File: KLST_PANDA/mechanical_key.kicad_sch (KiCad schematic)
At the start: 4 parts, among them SW5 BUTTON

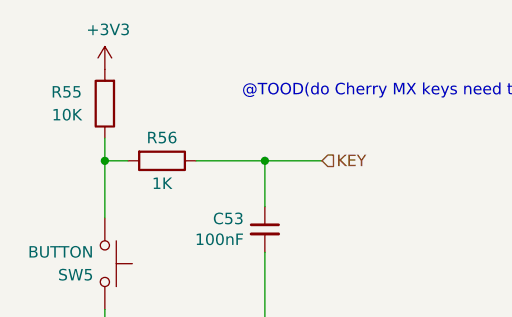
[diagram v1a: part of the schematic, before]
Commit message: started cleaning up schematic ( addressing DRC errors/warning ) (WIP)
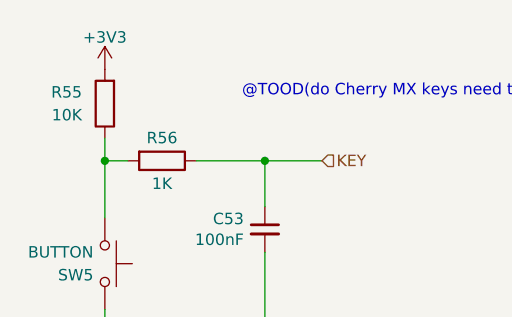
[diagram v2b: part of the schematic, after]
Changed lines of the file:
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@@
       (effects (font (size 1.27 1.27)) hide)
     )
-    (property "Value" "+3V3" (at 134.366 81.3308 0)
+    (property "Value" "+3V3" (at 133.985 82.169 0)
       (effects (font (size 1.27 1.27)))
     )
@@
         )
         (path "/b4513875-4c57-4720-bcc5-43ead67fe18f/f08ee185-46fd-4c64-8c0d-73017bc497ee/042452de-70bc-4b43-b264-a9a1cbea3e51"
-          (reference "#PWR090") (unit 1)
+          (reference "#PWR091") (unit 1)
         )
         (path "/b4513875-4c57-4720-bcc5-43ead67fe18f/f08ee185-46fd-4c64-8c0d-73017bc497ee/84723a09-c269-4794-b0be-89f4260a1140"
-          (reference "#PWR092") (unit 1)
+          (reference "#PWR093") (unit 1)
         )
       )
@@
         )
         (path "/b4513875-4c57-4720-bcc5-43ead67fe18f/f08ee185-46fd-4c64-8c0d-73017bc497ee/042452de-70bc-4b43-b264-a9a1cbea3e51"
-          (reference "#PWR091") (unit 1)
+          (reference "#PWR092") (unit 1)
         )
         (path "/b4513875-4c57-4720-bcc5-43ead67fe18f/f08ee185-46fd-4c64-8c0d-73017bc497ee/84723a09-c269-4794-b0be-89f4260a1140"
-          (reference "#PWR093") (unit 1)
+          (reference "#PWR094") (unit 1)
         )
       )

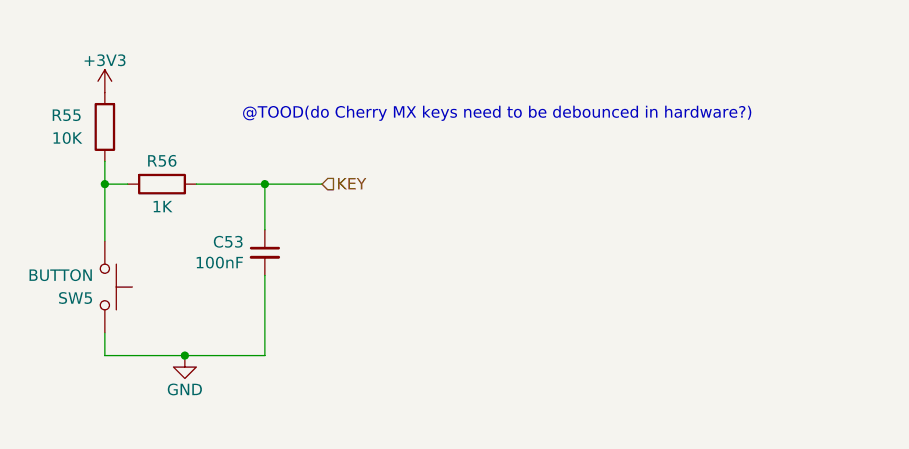
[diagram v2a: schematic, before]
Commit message: removed DRC warnings and error, added power page
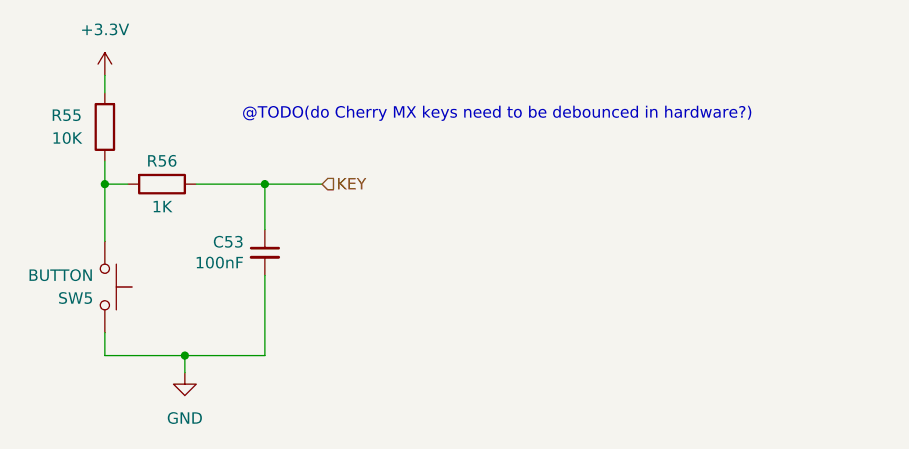
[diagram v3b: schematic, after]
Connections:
- net +3V3 renamed +3.3V
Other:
- note added: "@TODO(do Cherry MX keys need to be debounced in hardware?)"
- note removed: "@TOOD(do Cherry MX keys need to be debounced in hardware?)"
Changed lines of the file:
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@@
 (kicad_sch (version 20230121) (generator eeschema)
   (paper "A4")
+  (junction (at 133.985 95.885) (diameter 0) (color 0 0 0 0)
+  )
+  (junction (at 151.765 95.885) (diameter 0) (color 0 0 0 0)
+  )
   (junction (at 142.875 114.935) (diameter 0) (color 0 0 0 0)
   )
-  (junction (at 133.985 95.885) (diameter 0) (color 0 0 0 0)
-  )
-  (junction (at 151.765 95.885) (diameter 0) (color 0 0 0 0)
+  (wire (pts (xy 133.985 83.82) (xy 133.985 85.725))
+    (stroke (width 0) (type default))
+  )
+  (wire (pts (xy 142.875 114.935) (xy 151.765 114.935))
+    (stroke (width 0) (type default))
   )
   (wire (pts (xy 133.985 114.935) (xy 142.875 114.935))
@@
     (stroke (width 0) (type default))
   )
-  (wire (pts (xy 142.875 114.935) (xy 151.765 114.935))
-    (stroke (width 0) (type default))
-  )
   (wire (pts (xy 151.765 106.045) (xy 151.765 114.935))
     (stroke (width 0) (type default))
   )
+  (wire (pts (xy 142.875 114.935) (xy 142.875 116.84))
+    (stroke (width 0) (type default))
+  )
   (wire (pts (xy 144.145 95.885) (xy 151.765 95.885))
     (stroke (width 0) (type default))
@@
     (stroke (width 0) (type default))
   )
-  (text "@TOOD(do Cherry MX keys need to be debounced in hardware?)"
+  (text "@TODO(do Cherry MX keys need to be debounced in hardware?)"
     (at 149.225 88.9 0)
     (effects (font (size 1.27 1.27)) (justify left bottom))
@@
     (effects (font (size 1.27 1.27)) (justify left))
   )
-  (symbol (lib_id "power:+3V3") (at 133.985 85.725 0) (unit 1)
-    (in_bom yes) (on_board yes) (dnp no)
-    (property "Reference" "#PWR080" (at 133.985 89.535 0)
-      (effects (font (size 1.27 1.27)) hide)
-    )
-    (property "Value" "+3V3" (at 133.985 82.169 0)
-      (effects (font (size 1.27 1.27)))
-    )
-    (property "Footprint" "" (at 133.985 85.725 0)
-      (effects (font (size 1.27 1.27)) hide)
-    )
-    (property "Datasheet" "" (at 133.985 85.725 0)
-      (effects (font (size 1.27 1.27)) hide)
-    )
-    (pin "1")
-    (instances
-      (project "KLST_SHEEP"
-        (path "/7c1fd6fc-5c53-4ccb-a456-46fe6fc0bc71/00000000-0000-0000-0000-00006058fda0"
-          (reference "#PWR080") (unit 1)
-        )
-      )
-      (project "KLST_PANDA"
-        (path "/b4513875-4c57-4720-bcc5-43ead67fe18f/f08ee185-46fd-4c64-8c0d-73017bc497ee/7936a5e0-5a04-43e4-aa84-42432289d154"
-          (reference "#PWR071") (unit 1)
-        )
-        (path "/b4513875-4c57-4720-bcc5-43ead67fe18f/f08ee185-46fd-4c64-8c0d-73017bc497ee"
-          (reference "#PWR?") (unit 1)
-        )
-        (path "/b4513875-4c57-4720-bcc5-43ead67fe18f/f08ee185-46fd-4c64-8c0d-73017bc497ee/042452de-70bc-4b43-b264-a9a1cbea3e51"
-          (reference "#PWR091") (unit 1)
-        )
-        (path "/b4513875-4c57-4720-bcc5-43ead67fe18f/f08ee185-46fd-4c64-8c0d-73017bc497ee/84723a09-c269-4794-b0be-89f4260a1140"
-          (reference "#PWR093") (unit 1)
-        )
-      )
-    )
-  )
-  (symbol (lib_id "power:GND") (at 142.875 114.935 0) (unit 1)
-    (in_bom yes) (on_board yes) (dnp no)
-    (property "Reference" "#PWR081" (at 142.875 121.285 0)
-      (effects (font (size 1.27 1.27)) hide)
-    )
-    (property "Value" "GND" (at 142.875 118.745 0)
-      (effects (font (size 1.27 1.27)))
-    )
-    (property "Footprint" "" (at 142.875 114.935 0)
-      (effects (font (size 1.27 1.27)) hide)
-    )
-    (property "Datasheet" "" (at 142.875 114.935 0)
-      (effects (font (size 1.27 1.27)) hide)
-    )
-    (pin "1")
-    (instances
-      (project "KLST_SHEEP"
-        (path "/7c1fd6fc-5c53-4ccb-a456-46fe6fc0bc71/00000000-0000-0000-0000-00006058fda0"
-          (reference "#PWR081") (unit 1)
-        )
-      )
-      (project "KLST_PANDA"
-        (path "/b4513875-4c57-4720-bcc5-43ead67fe18f/f08ee185-46fd-4c64-8c0d-73017bc497ee/7936a5e0-5a04-43e4-aa84-42432289d154"
-          (reference "#PWR072") (unit 1)
-        )
-        (path "/b4513875-4c57-4720-bcc5-43ead67fe18f/f08ee185-46fd-4c64-8c0d-73017bc497ee"
-          (reference "#PWR?") (unit 1)
-        )
-        (path "/b4513875-4c57-4720-bcc5-43ead67fe18f/f08ee185-46fd-4c64-8c0d-73017bc497ee/042452de-70bc-4b43-b264-a9a1cbea3e51"
-          (reference "#PWR092") (unit 1)
-        )
-        (path "/b4513875-4c57-4720-bcc5-43ead67fe18f/f08ee185-46fd-4c64-8c0d-73017bc497ee/84723a09-c269-4794-b0be-89f4260a1140"
-          (reference "#PWR094") (unit 1)
+  (symbol (lib_id "power:+3.3V") (at 133.985 83.82 0) (unit 1)
+    (in_bom yes) (on_board yes) (dnp no) (fields_autoplaced)
+    (property "Reference" "#PWR077" (at 133.985 87.63 0)
+      (effects (font (size 1.27 1.27)) hide)
+    )
+    (property "Value" "+3.3V" (at 133.985 78.74 0)
+      (effects (font (size 1.27 1.27)))
+    )
+    (property "Footprint" "" (at 133.985 83.82 0)
+      (effects (font (size 1.27 1.27)) hide)
+    )
+    (property "Datasheet" "" (at 133.985 83.82 0)
+      (effects (font (size 1.27 1.27)) hide)
+    )
+    (pin "1")
+    (instances
+      (project "KLST_PANDA"
+        (path "/b4513875-4c57-4720-bcc5-43ead67fe18f/47e8e77e-c64e-4c44-bfd8-2073580a3d85"
+          (reference "#PWR077") (unit 1)
+        )
+        (path "/b4513875-4c57-4720-bcc5-43ead67fe18f/f08ee185-46fd-4c64-8c0d-73017bc497ee/042452de-70bc-4b43-b264-a9a1cbea3e51"
+          (reference "#PWR082") (unit 1)
+        )
+        (path "/b4513875-4c57-4720-bcc5-43ead67fe18f/f08ee185-46fd-4c64-8c0d-73017bc497ee/84723a09-c269-4794-b0be-89f4260a1140"
+          (reference "#PWR084") (unit 1)
+        )
+      )
+    )
+  )
+  (symbol (lib_id "power:GND") (at 142.875 116.84 0) (unit 1)
+    (in_bom yes) (on_board yes) (dnp no) (fields_autoplaced)
+    (property "Reference" "#PWR083" (at 142.875 123.19 0)
+      (effects (font (size 1.27 1.27)) hide)
+    )
+    (property "Value" "GND" (at 142.875 121.92 0)
+      (effects (font (size 1.27 1.27)))
+    )
+    (property "Footprint" "" (at 142.875 116.84 0)
+      (effects (font (size 1.27 1.27)) hide)
+    )
+    (property "Datasheet" "" (at 142.875 116.84 0)
+      (effects (font (size 1.27 1.27)) hide)
+    )
+    (pin "1")
+    (instances
+      (project "KLST_PANDA"
+        (path "/b4513875-4c57-4720-bcc5-43ead67fe18f/f08ee185-46fd-4c64-8c0d-73017bc497ee/042452de-70bc-4b43-b264-a9a1cbea3e51"
+          (reference "#PWR083") (unit 1)
+        )
+        (path "/b4513875-4c57-4720-bcc5-43ead67fe18f/f08ee185-46fd-4c64-8c0d-73017bc497ee/84723a09-c269-4794-b0be-89f4260a1140"
+          (reference "#PWR085") (unit 1)
         )
       )
@@
         )
         (path "/b4513875-4c57-4720-bcc5-43ead67fe18f/f08ee185-46fd-4c64-8c0d-73017bc497ee/042452de-70bc-4b43-b264-a9a1cbea3e51"
-          (reference "C71") (unit 1)
-        )
-        (path "/b4513875-4c57-4720-bcc5-43ead67fe18f/f08ee185-46fd-4c64-8c0d-73017bc497ee/84723a09-c269-4794-b0be-89f4260a1140"
-          (reference "C72") (unit 1)
+          (reference "C47") (unit 1)
+        )
+        (path "/b4513875-4c57-4720-bcc5-43ead67fe18f/f08ee185-46fd-4c64-8c0d-73017bc497ee/84723a09-c269-4794-b0be-89f4260a1140"
+          (reference "C48") (unit 1)
         )
       )
@@
         )
         (path "/b4513875-4c57-4720-bcc5-43ead67fe18f/f08ee185-46fd-4c64-8c0d-73017bc497ee/042452de-70bc-4b43-b264-a9a1cbea3e51"
-          (reference "R67") (unit 1)
-        )
-        (path "/b4513875-4c57-4720-bcc5-43ead67fe18f/f08ee185-46fd-4c64-8c0d-73017bc497ee/84723a09-c269-4794-b0be-89f4260a1140"
-          (reference "R69") (unit 1)
+          (reference "R53") (unit 1)
+        )
+        (path "/b4513875-4c57-4720-bcc5-43ead67fe18f/f08ee185-46fd-4c64-8c0d-73017bc497ee/84723a09-c269-4794-b0be-89f4260a1140"
+          (reference "R55") (unit 1)
         )
       )
@@
         )
         (path "/b4513875-4c57-4720-bcc5-43ead67fe18f/f08ee185-46fd-4c64-8c0d-73017bc497ee/042452de-70bc-4b43-b264-a9a1cbea3e51"
-          (reference "R68") (unit 1)
-        )
-        (path "/b4513875-4c57-4720-bcc5-43ead67fe18f/f08ee185-46fd-4c64-8c0d-73017bc497ee/84723a09-c269-4794-b0be-89f4260a1140"
-          (reference "R70") (unit 1)
-        )
-      )
+          (reference "R54") (unit 1)
+        )
+        (path "/b4513875-4c57-4720-bcc5-43ead67fe18f/f08ee185-46fd-4c64-8c0d-73017bc497ee/84723a09-c269-4794-b0be-89f4260a1140"
+          (reference "R56") (unit 1)
+        )
+      )

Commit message: cleaned up
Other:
- moved on the sheet: C53, R56, SW5
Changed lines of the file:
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@@
     (stroke (width 0) (type default))
   )
-  (wire (pts (xy 151.765 95.885) (xy 151.765 100.965))
-    (stroke (width 0) (type default))
-  )
-  (wire (pts (xy 151.765 106.045) (xy 151.765 114.935))
+  (wire (pts (xy 151.765 95.885) (xy 151.765 102.87))
+    (stroke (width 0) (type default))
+  )
+  (wire (pts (xy 151.765 107.95) (xy 151.765 114.935))
     (stroke (width 0) (type default))
   )
@@
     (stroke (width 0) (type default))
   )
-  (wire (pts (xy 144.145 95.885) (xy 151.765 95.885))
-    (stroke (width 0) (type default))
-  )
-  (wire (pts (xy 133.985 95.885) (xy 133.985 102.235))
-    (stroke (width 0) (type default))
-  )
-  (wire (pts (xy 133.985 114.935) (xy 133.985 112.395))
-    (stroke (width 0) (type default))
-  )
-  (wire (pts (xy 136.525 95.885) (xy 133.985 95.885))
+  (wire (pts (xy 146.685 95.885) (xy 151.765 95.885))
+    (stroke (width 0) (type default))
+  )
+  (wire (pts (xy 133.985 95.885) (xy 133.985 100.33))
+    (stroke (width 0) (type default))
+  )
+  (wire (pts (xy 133.985 114.935) (xy 133.985 110.49))
+    (stroke (width 0) (type default))
+  )
+  (wire (pts (xy 139.065 95.885) (xy 133.985 95.885))
     (stroke (width 0) (type default))
   )
@@
     )
   )
-  (symbol (lib_id "Switch:SW_Push") (at 133.985 107.315 270) (unit 1)
-    (in_bom yes) (on_board yes) (dnp no)
-    (property "Reference" "SW5" (at 132.715 108.585 90)
+  (symbol (lib_id "Switch:SW_Push") (at 133.985 105.41 270) (unit 1)
+    (in_bom yes) (on_board yes) (dnp no)
+    (property "Reference" "SW5" (at 132.715 106.68 90)
       (effects (font (size 1.27 1.27)) (justify right))
     )
-    (property "Value" "BUTTON" (at 132.715 106.045 90)
+    (property "Value" "BUTTON" (at 132.715 104.14 90)
       (effects (font (size 1.27 1.27)) (justify right))
     )
-    (property "Footprint" "Cherry_MX:SW_Cherry_MX_PCB" (at 139.065 107.315 0)
-      (effects (font (size 1.27 1.27)) hide)
-    )
-    (property "Datasheet" "~" (at 139.065 107.315 0)
+    (property "Footprint" "Cherry_MX:SW_Cherry_MX_PCB" (at 139.065 105.41 0)
+      (effects (font (size 1.27 1.27)) hide)
+    )
+    (property "Datasheet" "~" (at 139.065 105.41 0)
       (effects (font (size 1.27 1.27)) hide)
     )
@@
     )
   )
-  (symbol (lib_id "Device:C_Small") (at 151.765 103.505 0) (mirror y) (unit 1)
-    (in_bom yes) (on_board yes) (dnp no)
-    (property "Reference" "C53" (at 149.4282 102.3366 0)
-      (effects (font (size 1.27 1.27)) (justify left))
-    )
-    (property "Value" "100nF" (at 149.4282 104.648 0)
-      (effects (font (size 1.27 1.27)) (justify left))
-    )
-    (property "Footprint" "Capacitor_SMD:C_0402_1005Metric" (at 151.765 103.505 0)
-      (effects (font (size 1.27 1.27)) hide)
-    )
-    (property "Datasheet" "~" (at 151.765 103.505 0)
-      (effects (font (size 1.27 1.27)) hide)
-    )
-    (property "MFR.Part #" "CL05B104KO5NNNC" (at 151.765 103.505 0)
-      (effects (font (size 1.27 1.27)) hide)
-    )
-    (property "LCSC Part #" "" (at 151.765 103.505 0)
-      (effects (font (size 1.27 1.27)) hide)
-    )
-    (property "Extended Part" "-" (at 151.765 103.505 0)
-      (effects (font (size 1.27 1.27)) hide)
-    )
-    (property "JLCPCB Part #" "C1525" (at 151.765 103.505 0)
+  (symbol (lib_id "Device:C_Small") (at 151.765 105.41 0) (mirror y) (unit 1)
+    (in_bom yes) (on_board yes) (dnp no)
+    (property "Reference" "C53" (at 149.4282 104.2416 0)
+      (effects (font (size 1.27 1.27)) (justify left))
+    )
+    (property "Value" "100nF" (at 149.4282 106.553 0)
+      (effects (font (size 1.27 1.27)) (justify left))
+    )
+    (property "Footprint" "Capacitor_SMD:C_0402_1005Metric" (at 151.765 105.41 0)
+      (effects (font (size 1.27 1.27)) hide)
+    )
+    (property "Datasheet" "~" (at 151.765 105.41 0)
+      (effects (font (size 1.27 1.27)) hide)
+    )
+    (property "MFR.Part #" "CL05B104KO5NNNC" (at 151.765 105.41 0)
+      (effects (font (size 1.27 1.27)) hide)
+    )
+    (property "LCSC Part #" "" (at 151.765 105.41 0)
+      (effects (font (size 1.27 1.27)) hide)
+    )
+    (property "Extended Part" "-" (at 151.765 105.41 0)
+      (effects (font (size 1.27 1.27)) hide)
+    )
+    (property "JLCPCB Part #" "C1525" (at 151.765 105.41 0)
       (effects (font (size 1.27 1.27)) hide)
     )
@@
     )
   )
-  (symbol (lib_id "Device:R") (at 140.335 95.885 270) (unit 1)
-    (in_bom yes) (on_board yes) (dnp no)
-    (property "Reference" "R56" (at 140.335 93.345 90)
-      (effects (font (size 1.27 1.27)))
-    )
-    (property "Value" "1K" (at 140.335 98.425 90)
-      (effects (font (size 1.27 1.27)))
-    )
-    (property "Footprint" "Resistor_SMD:R_0402_1005Metric" (at 140.335 94.107 90)
-      (effects (font (size 1.27 1.27)) hide)
-    )
-    (property "Datasheet" "~" (at 140.335 95.885 0)
-      (effects (font (size 1.27 1.27)) hide)
-    )
-    (property "MFR.Part #" "0402WGF1001TCE" (at 140.335 95.885 90)
-      (effects (font (size 1.27 1.27)) hide)
-    )
-    (property "LCSC Part #" "" (at 140.335 95.885 0)
-      (effects (font (size 1.27 1.27)) hide)
-    )
-    (property "Extended Part" "-" (at 140.335 95.885 0)
-      (effects (font (size 1.27 1.27)) hide)
-    )
-    (property "JLCPCB Part #" "C11702" (at 140.335 95.885 0)
-      (effects (font (size 1.27 1.27)) hide)
-    )
+  (symbol (lib_id "Device:R") (at 142.875 95.885 270) (unit 1)
+    (in_bom yes) (on_board yes) (dnp no)
+    (property "Reference" "R56" (at 142.875 93.345 90)
+      (effects (font (size 1.27 1.27)))
+    )
+    (property "Value" "1K" (at 142.875 98.425 90)
+      (effects (font (size 1.27 1.27)))
+    )
+    (property "Footprint" "Resistor_SMD:R_0402_1005Metric" (at 142.875 94.107 90)
+      (effects (font (size 1.27 1.27)) hide)
+    )
+    (property "Datasheet" "~" (at 142.875 95.885 0)
+      (effects (font (size 1.27 1.27)) hide)
+    )
+    (property "MFR.Part #" "0402WGF1001TCE" (at 142.875 95.885 90)
+      (effects (font (size 1.27 1.27)) hide)
+    )
+    (property "LCSC Part #" "" (at 142.875 95.885 0)
+      (effects (font (size 1.27 1.27)) hide)
+    )
+    (property "Extended Part" "-" (at 142.875 95.885 0)
+      (effects (font (size 1.27 1.27)) hide)
+    )
+    (property "JLCPCB Part #" "C11702" (at 142.875 95.885 0)
+      (effects (font (size 1.27 1.27)) hide)
+    )

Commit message: started spec'ing components
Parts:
- C53: JLCPCB (none) -> C1525; JLCPCB Part # C1525 -> (none)
- R55: JLCPCB (none) -> C25744; JLCPCB Part # C25744 -> (none)
- R56: JLCPCB (none) -> C11702; JLCPCB Part # C11702 -> (none)
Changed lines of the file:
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@@
       (effects (font (size 1.27 1.27)) hide)
     )
-    (property "JLCPCB Part #" "C1525" (at 151.765 105.41 0)
+    (property "JLCPCB Part #" "" (at 151.765 105.41 0)
+      (effects (font (size 1.27 1.27)) hide)
+    )
+    (property "JLCPCB" "C1525" (at 151.765 105.41 0)
+      (effects (font (size 1.27 1.27)) hide)
+    )
+    (property "Description" "16V" (at 151.765 105.41 0)
       (effects (font (size 1.27 1.27)) hide)
     )
@@
       (effects (font (size 1.27 1.27)) hide)
     )
-    (property "JLCPCB Part #" "C25744" (at 133.985 89.535 0)
+    (property "JLCPCB Part #" "" (at 133.985 89.535 0)
+      (effects (font (size 1.27 1.27)) hide)
+    )
+    (property "JLCPCB" "C25744" (at 133.985 89.535 0)
       (effects (font (size 1.27 1.27)) hide)
     )
@@
       (effects (font (size 1.27 1.27)) hide)
     )
-    (property "JLCPCB Part #" "C11702" (at 142.875 95.885 0)
+    (property "JLCPCB Part #" "" (at 142.875 95.885 0)
       (effects (font (size 1.27 1.27)) hide)
     )
+    (property "JLCPCB" "C11702" (at 142.875 95.885 0)
+      (effects (font (size 1.27 1.27)) hide)
+    )
